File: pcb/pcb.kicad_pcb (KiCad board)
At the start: 2 copper layers, 100 x 70 mm, 27 parts, among them J1 PJ301M-12, J2 PJ301M-12, J3 PJ301M-12, SW1 12x12 Tactile, SW2 12x12 Tactile, SW3 12x12 Tactile, SW4 12x12 Tactile, SW5 12x12 Tactile, SW6 12x12 Tactile, SW7 12x12 Tactile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

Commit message: Finish Rev 1
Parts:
- moved D2 10.8 mm to (183.1, 72.5)
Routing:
- net GND: track 0.00 -> 328.8 mm
- net +5V: track 0.00 -> 113.0 mm
- net SW_8: track 0.00 -> 104.2 mm
- net SW_5: track 0.00 -> 95.4 mm
- net SW_6: track 0.00 -> 85.2 mm, vias 0 -> 1
- net SDI: track 0.00 -> 81.5 mm, vias 0 -> 1
- net SW_7: track 0.00 -> 79.6 mm
- net CS: track 0.00 -> 77.0 mm
- net Net-(D1-A): track 0.00 -> 74.3 mm
- net SW_4: track 0.00 -> 71.8 mm
- net RX: track 0.00 -> 70.4 mm
- net Net-(J3-Pad3): track 0.00 -> 65.7 mm
- net SCK: track 0.00 -> 60.2 mm
- net Net-(C1-Pad1): track 0.00 -> 56.5 mm, vias 0 -> 1
- net SW_3: track 0.00 -> 54.4 mm
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- added copper zone on B.Cu, net GND
- added copper zone on F.Cu, net GND

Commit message: Revert MIDI jack
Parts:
- removed JP2: Jumper, Jumper:SolderJumper-2_P1.3mm_Open_RoundedPad1.0x1.5mm
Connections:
- J3 pad 1: Net-(JP2-A) -> GND
- J3 pad 2: Net-(D1-A) -> Net-(J3-Pad2)
- J3 pad 3: Net-(J3-Pad3) -> Net-(D1-A)
- R4 pad 2: Net-(J3-Pad3) -> Net-(J3-Pad2)
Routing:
- net Net-(J3-Pad3): track 65.7 -> 0.00 mm
- net Net-(J3-Pad2): track 0.00 -> 64.7 mm
- net GND: track 328.8 -> 310.7 mm
- net Net-(JP2-A): track 17.4 -> 0.00 mm
- net Net-(D1-A): track 74.3 -> 90.8 mm

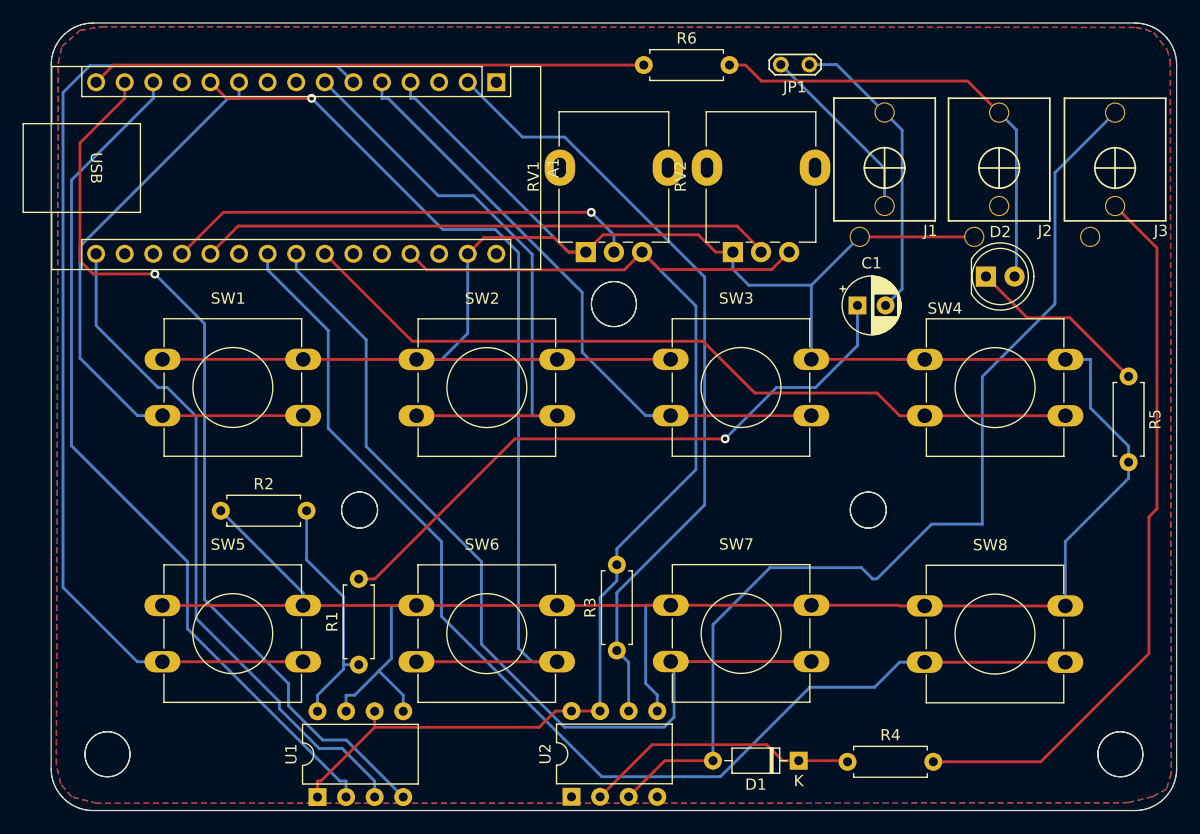
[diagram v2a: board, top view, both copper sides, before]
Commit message: Fix clock output
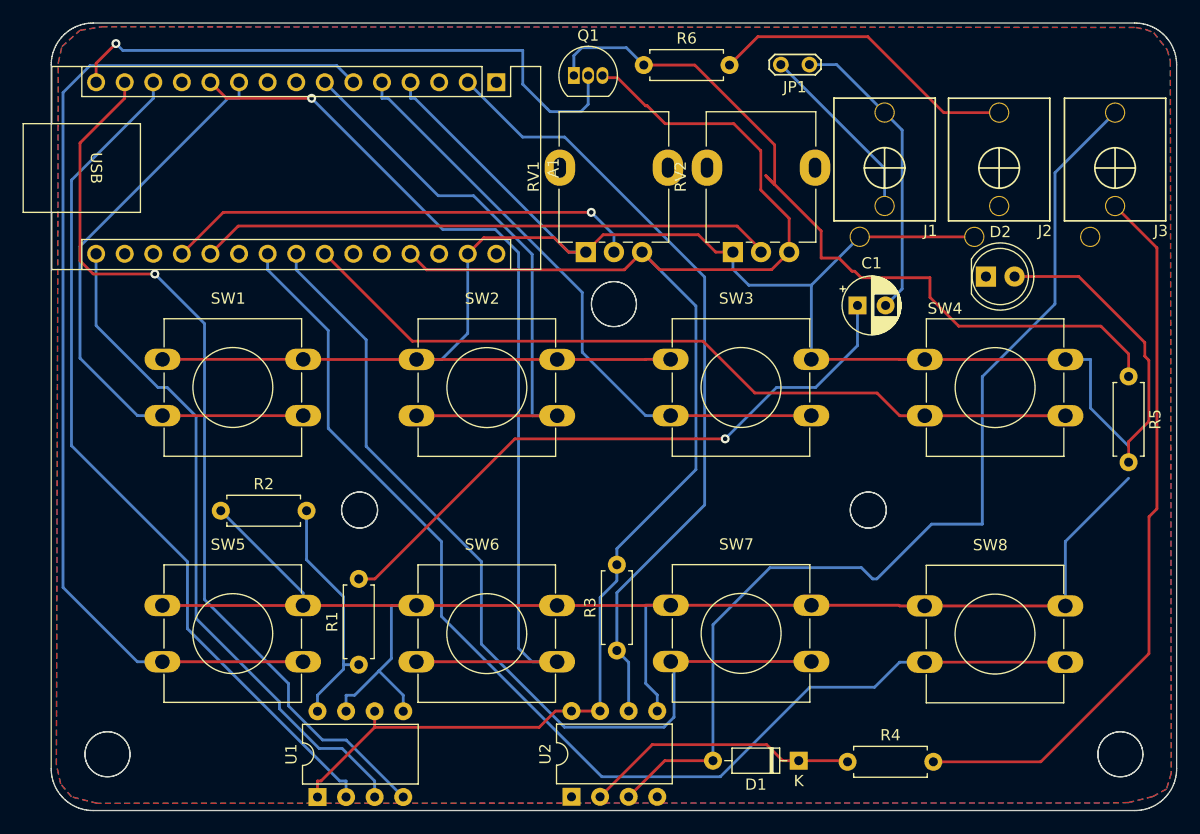
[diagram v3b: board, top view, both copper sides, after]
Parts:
- added Q1: 2N3904, Package_TO_SOT_THT:TO-92_Inline, F.Cu at (146.4, 54.7)
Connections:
- D2 pad 1: Net-(D2-K) -> GND
- J2 pad 3: Net-(D2-A) -> Net-(J2-Pad3)
- R5 pad 1: Net-(D2-K) -> Net-(Q1-E)
- R5 pad 2: GND -> Net-(D2-A)
- R6 pad 1: CLOCK_OUT -> Net-(Q1-E)
- R6 pad 2: Net-(D2-A) -> Net-(J2-Pad3)
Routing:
- net Net-(Q1-E): track 0.00 -> 71.3 mm
- net Net-(J2-Pad3): track 0.00 -> 27.8 mm
- net +5V: track 113.0 -> 139.9 mm
- net Net-(D2-K): track 16.4 -> 0.00 mm
- net Net-(D2-A): track 40.7 -> 25.5 mm
- net CLOCK_OUT: track 49.3 -> 53.2 mm, vias 0 -> 1
- net GND: track 310.7 -> 307.8 mm
